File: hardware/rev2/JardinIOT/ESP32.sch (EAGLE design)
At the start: 9 parts, among them IC1 7815TV

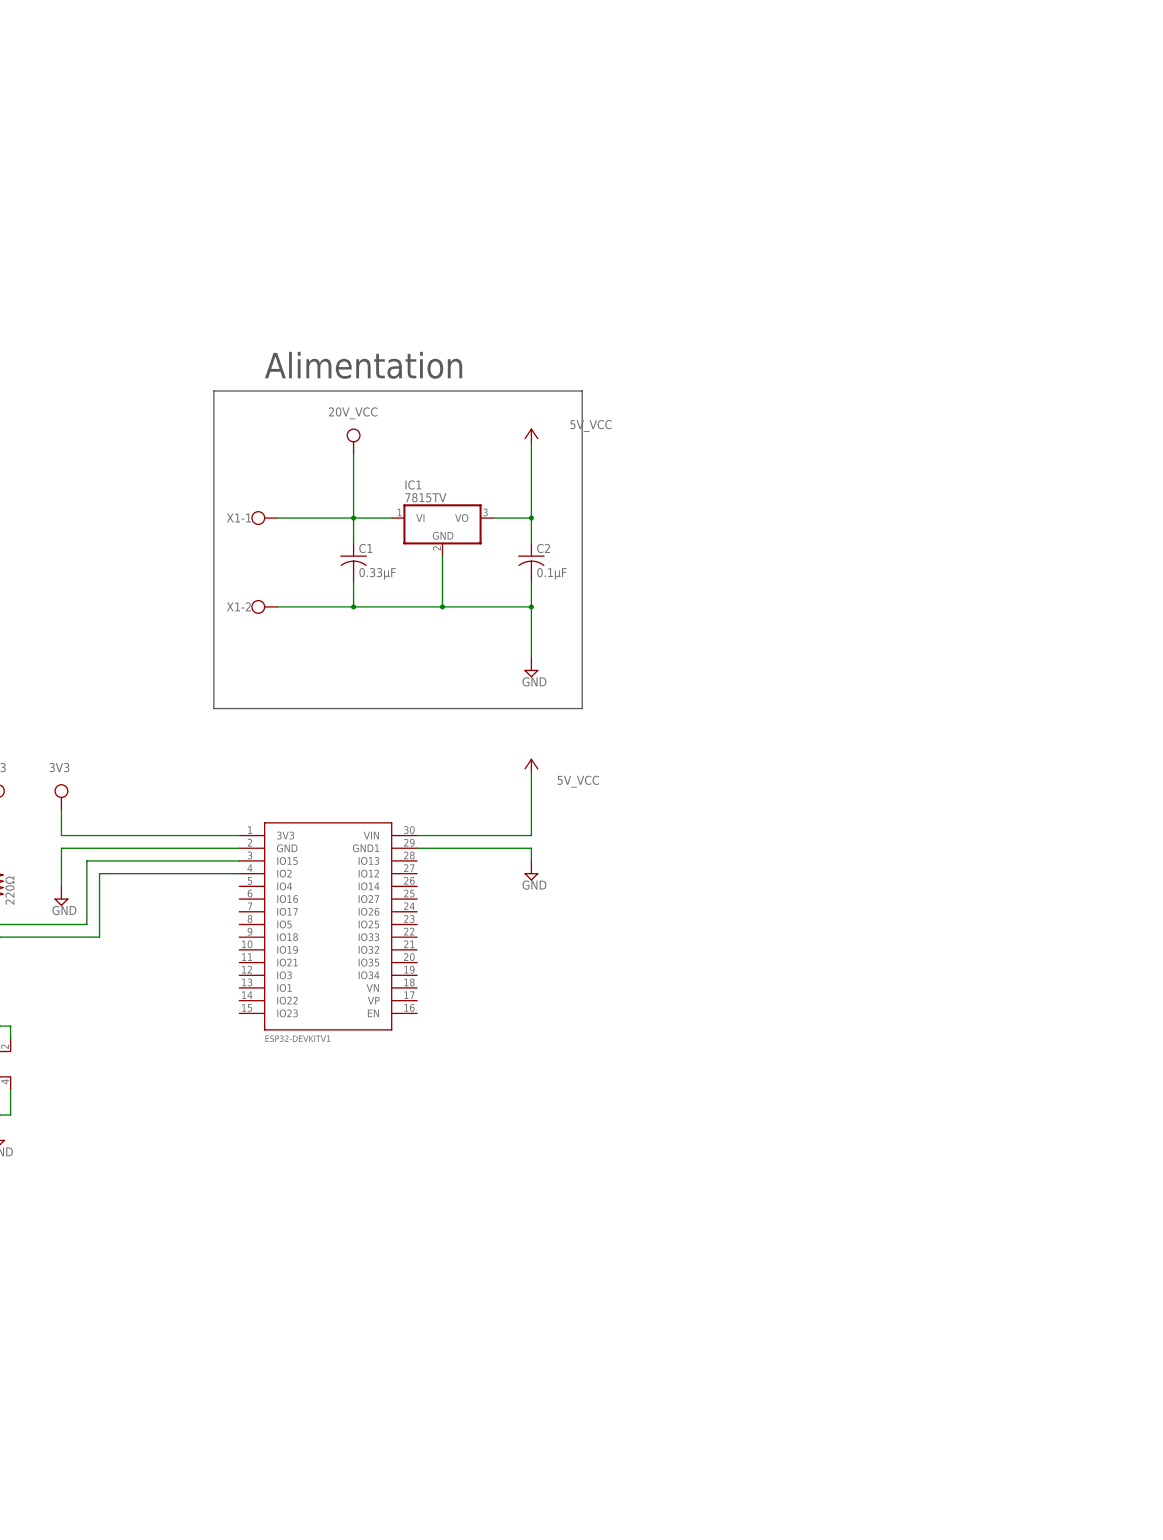
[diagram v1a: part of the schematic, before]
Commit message: Ajout des borniers à vis pour les capteurs et actionneurs
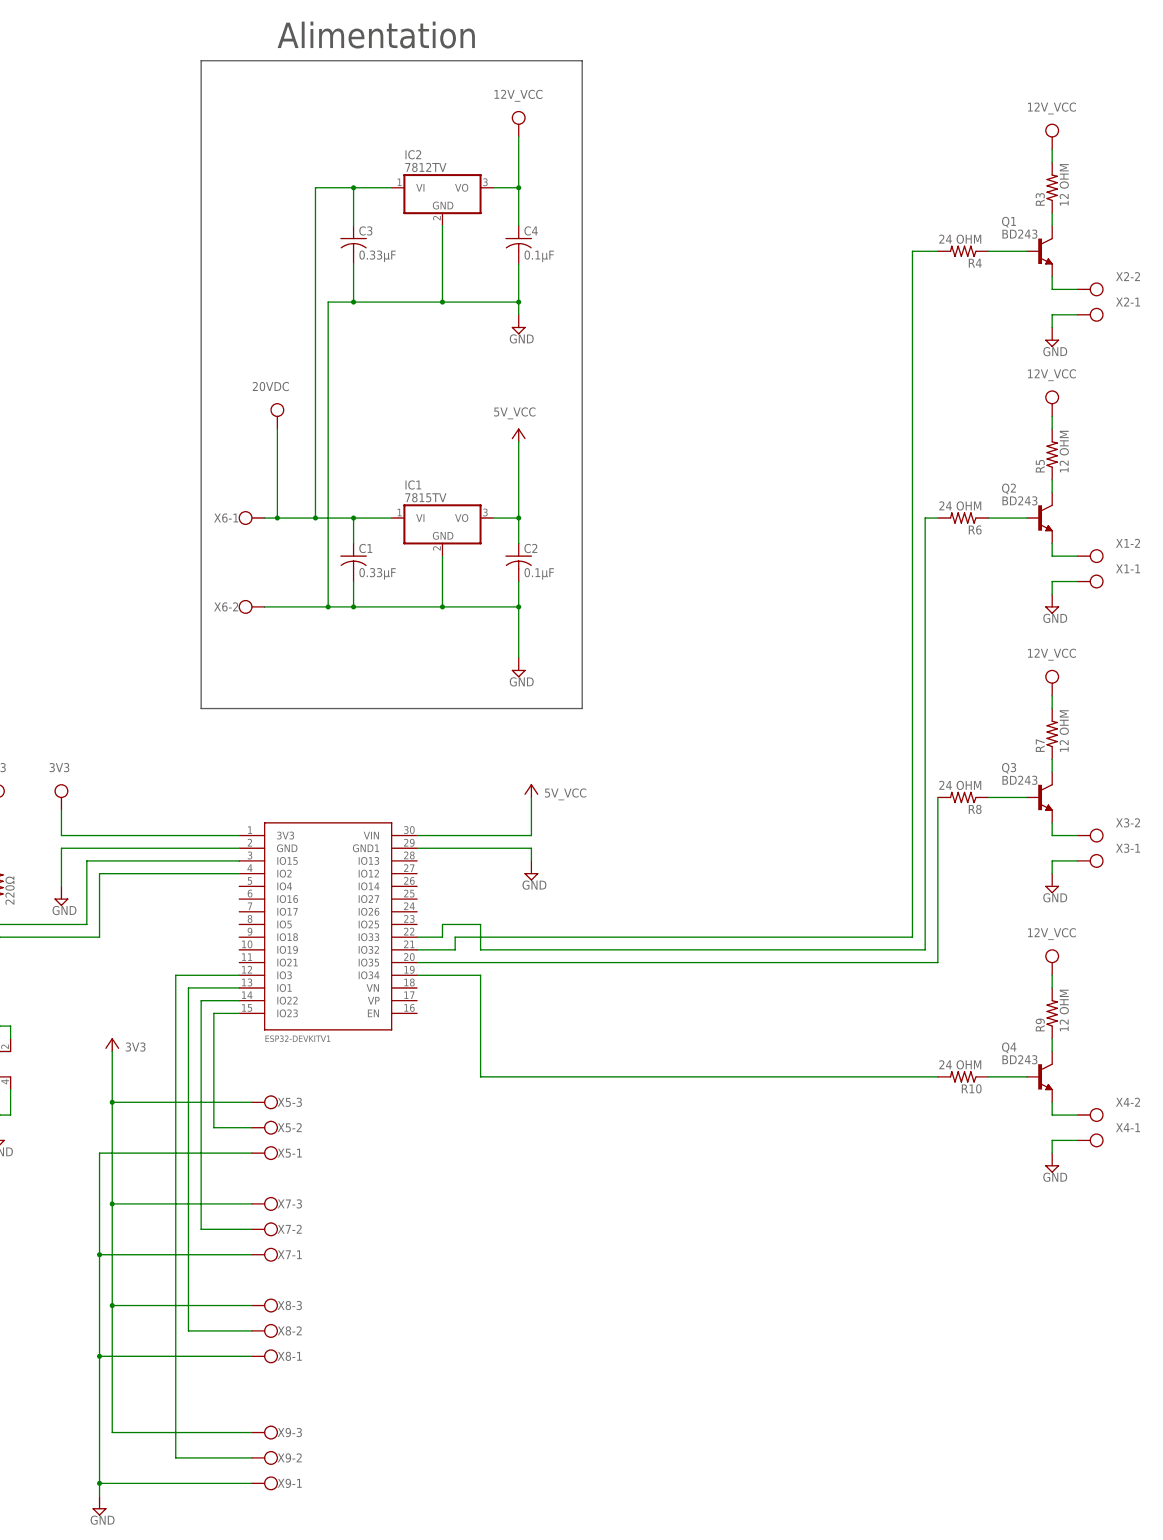
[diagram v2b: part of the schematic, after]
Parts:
- added C3: 0.33µF, rcl:C-USC0805
- added C4: 0.1µF, rcl:C-USC0805
- added IC2: 7812TV, linear:7812TV
- added Q1, Q2, Q3, Q4: BD243, transistor-npn:BD243
- added R10, R4, R6, R8: 24 OHM, rcl:R-US_0204/7
- added R3, R5, R7, R9: 12 OHM, rcl:R-US_0204/7
- added X2, X3, X4, X6: (no value), con-wago-500:W237-102
- added X5, X7, X8, X9: (no value), con-wago-500:W237-103
- X1: device con-wago-500:W237-113 -> con-wago-500:W237-102
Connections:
- removed net 20V_VCC: C1.1, IC1.VI, X1-1.KL
- new net 12V_VCC: C4.1, IC2.VO, R3.2, R5.2, R7.2, R9.2
- new net 20VDC: C1.1, C3.1, IC1.VI, IC2.VI, X6-1.KL
- new net N$10: Q3.C, R7.1
- new net N$11: Q3.B, R8.1
- new net N$12: Q4.E, X4-2.KL
- new net N$13: Q4.C, R9.1
- new net N$14: Q4.B, R10.1
- new net N$15: R10.2, U$1.IO34
- new net N$16: U$1.IO23, X5-2.KL
- new net N$17: R8.2, U$1.IO35
- new net N$18: R6.2, U$1.IO33
- new net N$19: R4.2, U$1.IO32
- new net N$2: Q1.E, X2-2.KL
- new net N$20: U$1.IO22, X7-2.KL
- new net N$21: U$1.IO1, X8-2.KL
- new net N$22: U$1.IO3, X9-2.KL
- new net N$4: Q1.C, R3.1
- new net N$5: Q1.B, R4.1
- new net N$6: Q2.E, X1-2.KL
- new net N$7: Q2.C, R5.1
- new net N$8: Q2.B, R6.1
- new net N$9: Q3.E, X3-2.KL
- net 3V3: now also X5-3.KL, X7-3.KL, X8-3.KL, X9-3.KL
- net GND: now also C3.2, C4.2, IC2.GND, X1-1.KL, X2-1.KL, X3-1.KL, X4-1.KL, X5-1.KL, X6-2.KL, X7-1.KL, X8-1.KL, X9-1.KL; no longer X1-2.KL
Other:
- moved on the sheet: C2, X1-1, X1-2

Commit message: Meilleur mappage des broches du ESP32 sur le PCB
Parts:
- IC1: value 7815TV -> 7805TV; device linear:7815TV -> linear:7805TV
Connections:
- net N$1: now also U$1.IO2; no longer U$1.IO15
- net N$15: now also R4.2, U$1.IO17; no longer R10.2, U$1.IO34
- net N$16: now also U$1.IO33; no longer U$1.IO23
- net N$17: now also U$1.IO16; no longer U$1.IO35
- net N$18: now also U$1.IO5; no longer U$1.IO33
- net N$19: now also R10.2, U$1.IO4; no longer R4.2, U$1.IO32
- net N$20: now also U$1.IO32; no longer U$1.IO22
- net N$21: now also U$1.IO35; no longer U$1.IO1
- net N$22: now also U$1.IO34; no longer U$1.IO3
- net N$3: now also U$1.IO15; no longer U$1.IO2
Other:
- moved on the sheet: Q1, Q2, Q3, Q4, R10, R3, R4, R5, R6, R7, R8, R9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
